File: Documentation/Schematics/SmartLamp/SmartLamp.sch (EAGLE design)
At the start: 34 parts, among them J1 POWER_JACKPTH_BREAD, Q1 STN4NF03L, Q2 STN4NF03L, Q3 STN4NF03L, U1 MIC2920A, U2 DS3231MZ, U3 ATMEGA8/168/328, U4 HM-10, X1 16MHz

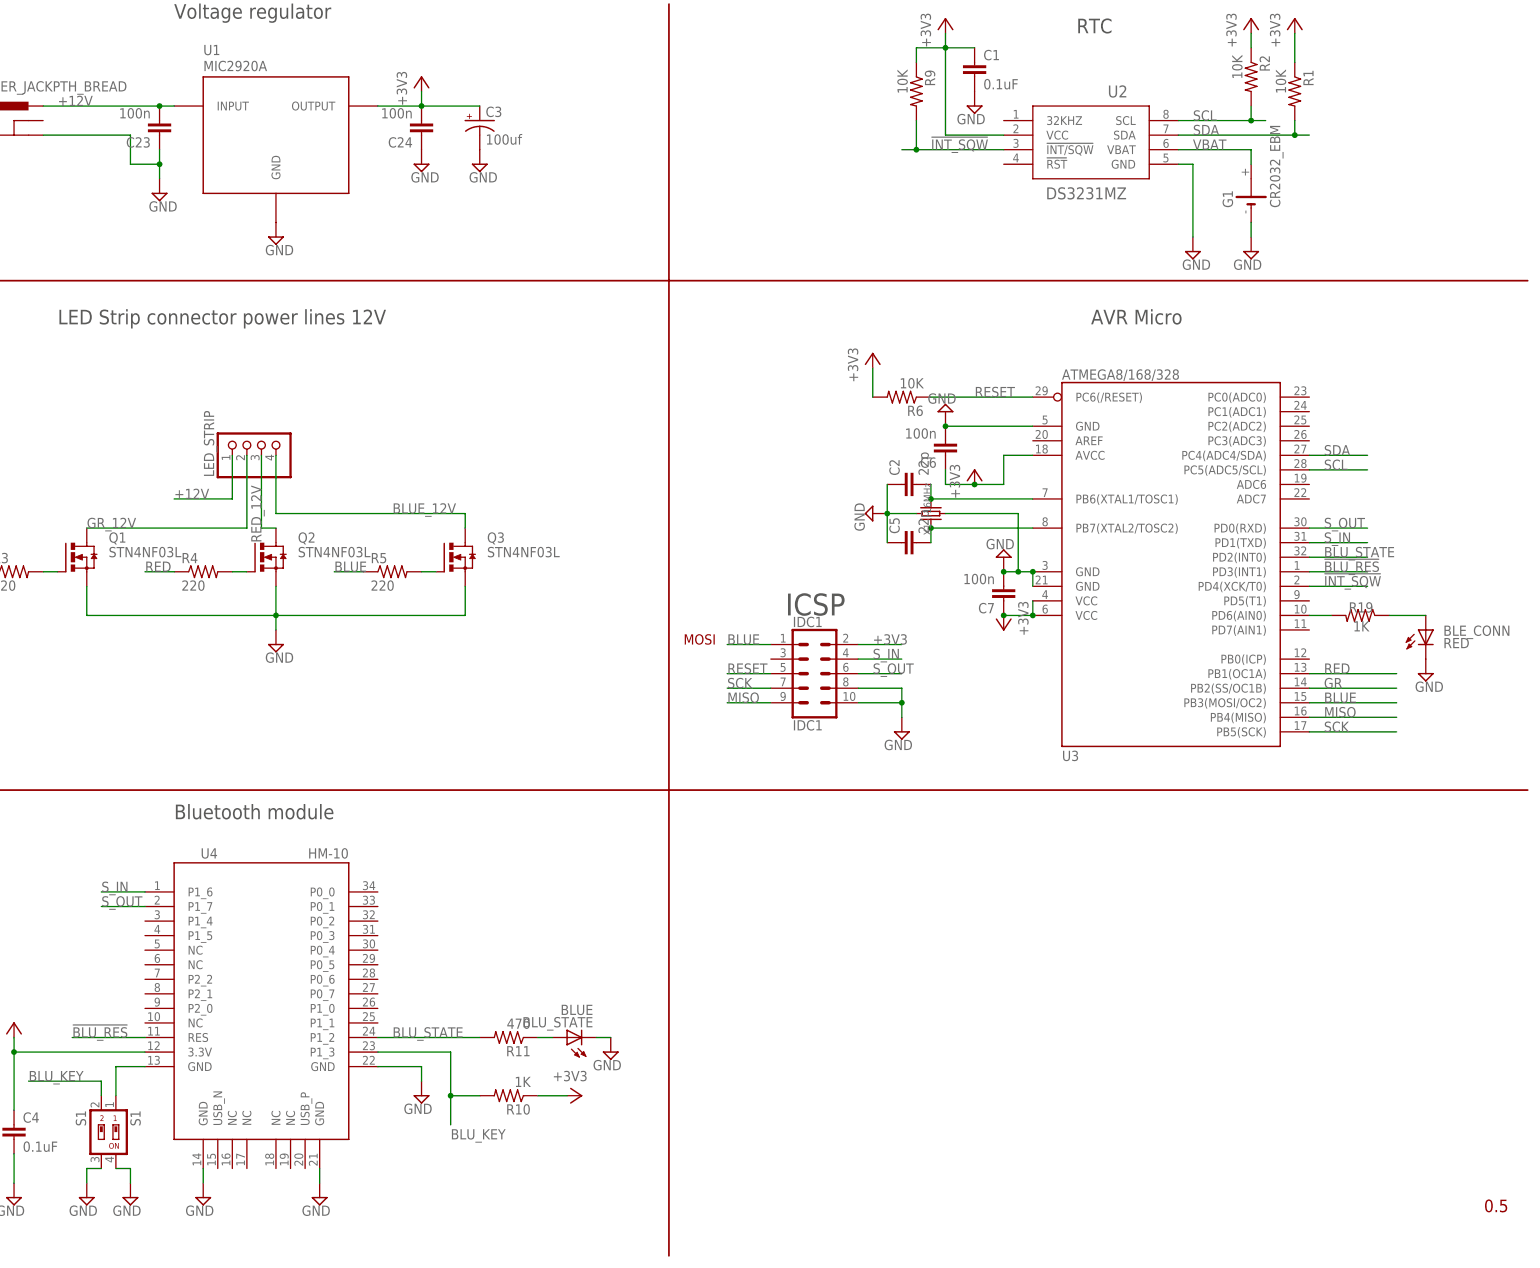
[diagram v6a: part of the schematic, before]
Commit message: Completet BOM, remove crystal (at 3.3v 16Mhz is not supported), fixed resistor value, added output pin for LED in main code
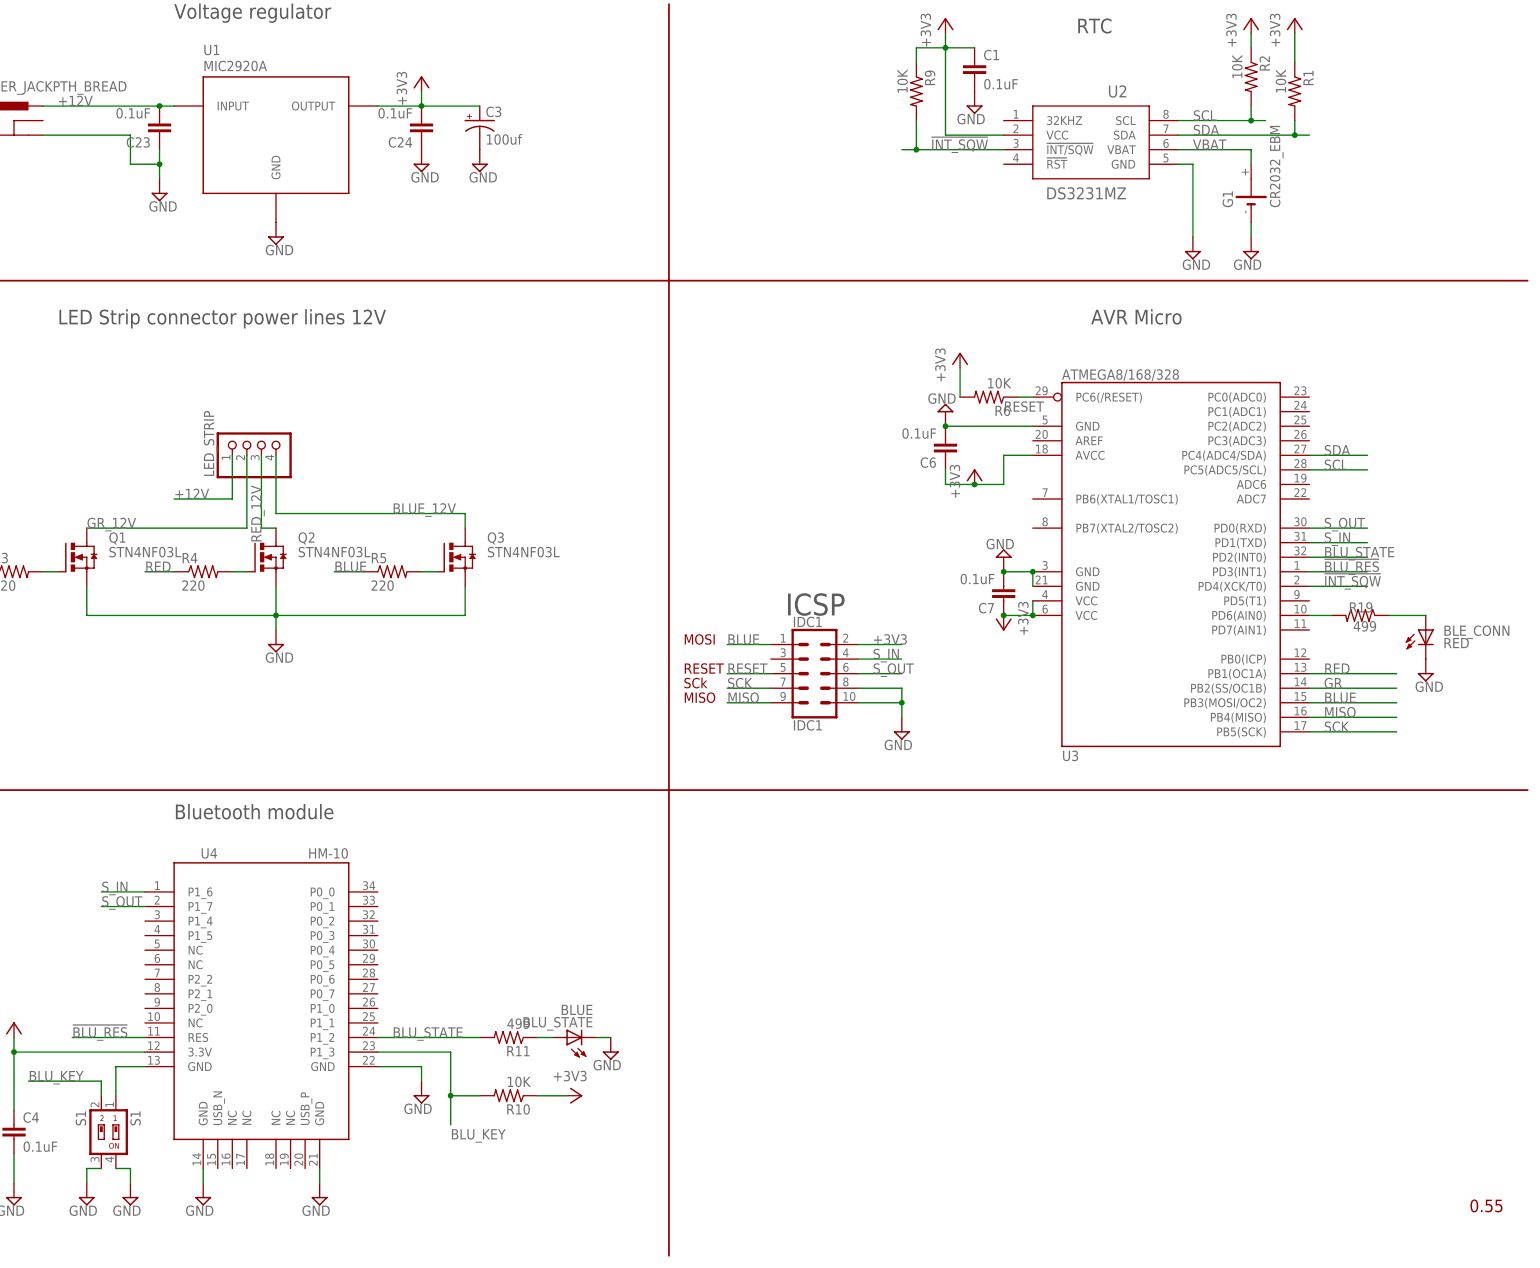
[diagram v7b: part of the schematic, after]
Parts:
- removed C2, C5: 22p, rcl:C-EUC0805
- removed X1: 16MHz, Discrete:CRYSTAL'3225'
- BLE_CONN, BLU_STATE: device adafruit:LEDCHIP-LED0805 -> adafruit:LEDCHIPLED_1206
- C1, C4: device rcl:C-EUC0805 -> rcl:C-EUC1206
- C23, C24, C6, C7: value 100n -> 0.1uF; device rcl:C-EUC0805 -> rcl:C-EUC1206
- R1, R2, R3, R4, R5, R6, R9: device rcl:R-US_R0805 -> rcl:R-US_R1206
- R10: value 1K -> 10K; device rcl:R-US_R0805 -> rcl:R-US_R1206
- R11: value 470 -> 499; device rcl:R-US_R0805 -> rcl:R-US_R1206
- R19: value 1K -> 499; device rcl:R-US_R0805 -> rcl:R-US_R1206
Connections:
- removed net N$15: C2.2, U3.PB6(XTAL1/TOSC1), X1.2
- removed net N$21: C5.2, U3.PB7(XTAL2/TOSC2), X1.1
- net GND: no longer C2.1, C5.1, X1.GND_BOTTOM, X1.GND_TOP
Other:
- note added: "MISO"
- note added: "RESET"
- note added: "SCk"
- moved on the sheet: R6

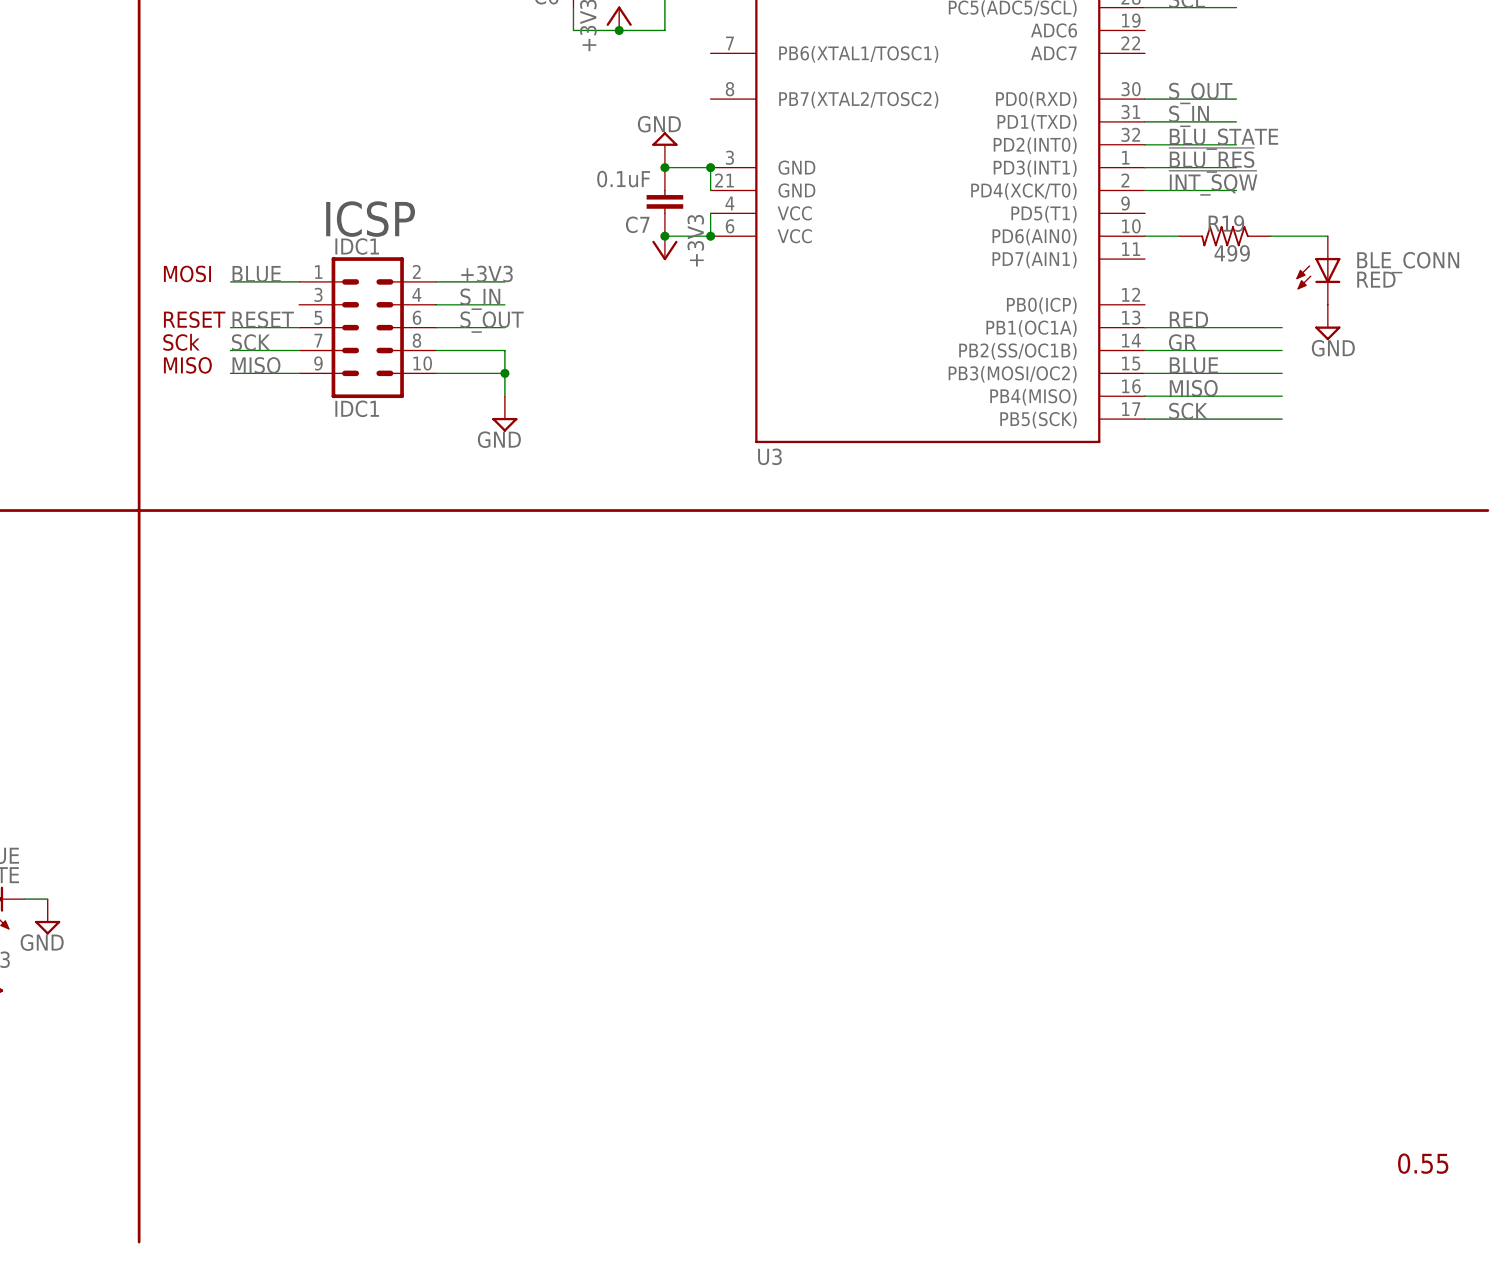
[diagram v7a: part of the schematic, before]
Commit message: Updated schetaic, board and partlit with AVR ISP connector and MOSFET on the bottom layer
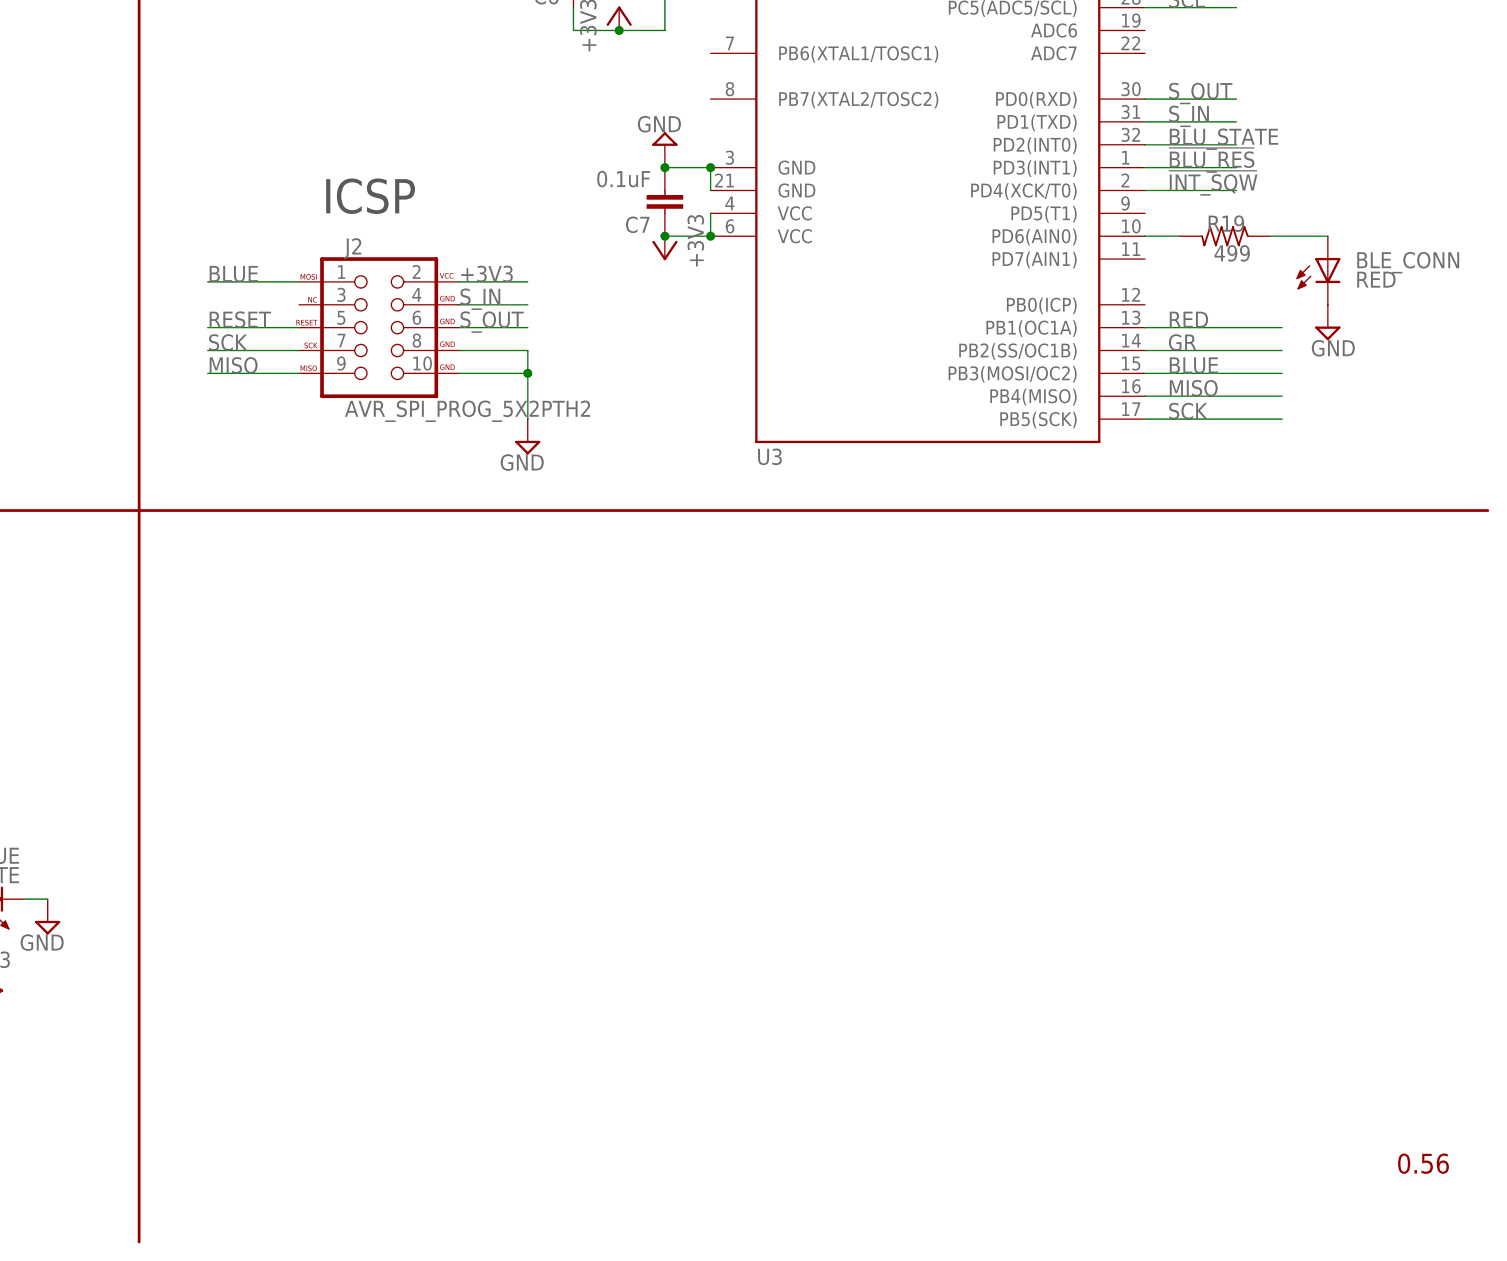
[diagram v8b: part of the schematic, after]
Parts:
- removed IDC1: IDC1, SparkFun-Connectors:CONN_05X2SHD
- added J2: AVR_SPI_PROG_5X2PTH2, SparkFun-Connectors:AVR_SPI_PROG_5X2PTH2
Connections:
- net +3V3: now also J2.VCC; no longer IDC1.2
- net BLUE: now also J2.MOSI; no longer IDC1.1
- net GND: now also J2.GND@3, J2.GND@4; no longer IDC1.10, IDC1.8
- net MISO: now also J2.MISO; no longer IDC1.9
- net RESET: now also J2.RESET; no longer IDC1.5
- net SCK: now also J2.SCK; no longer IDC1.7
- net S_IN: now also J2.GND@1; no longer IDC1.4
- net S_OUT: now also J2.GND@2; no longer IDC1.6
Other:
- note removed: "MISO"
- note removed: "MOSI"
- note removed: "RESET"
- note removed: "SCk"
